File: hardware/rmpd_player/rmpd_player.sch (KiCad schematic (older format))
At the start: 7 parts

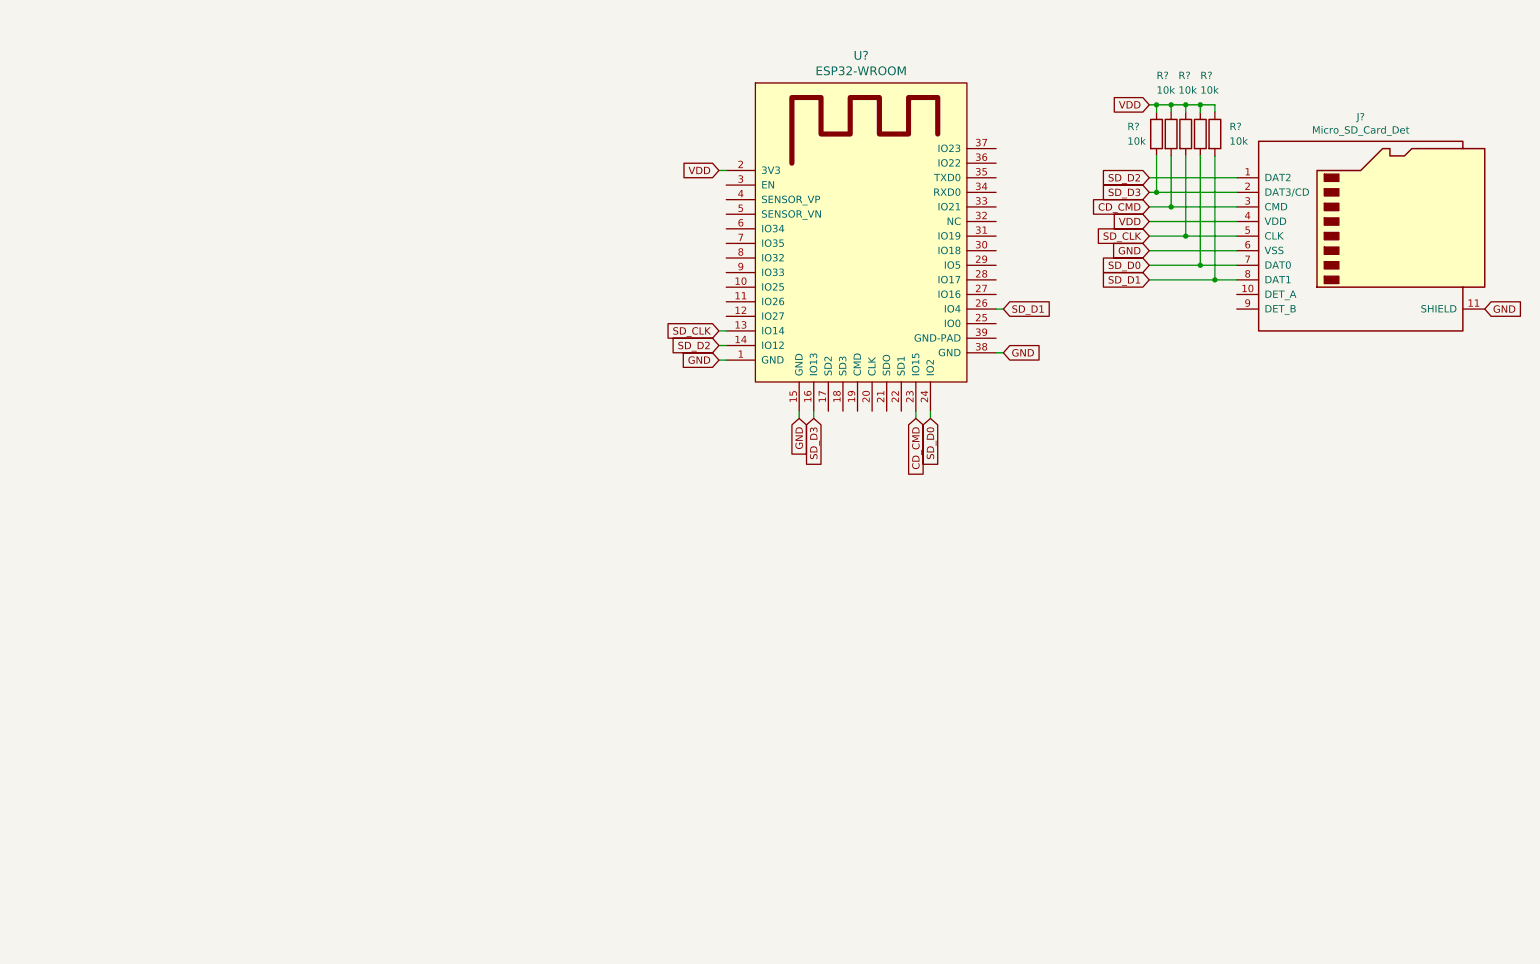
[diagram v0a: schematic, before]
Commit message: more schematic; vs1011 library
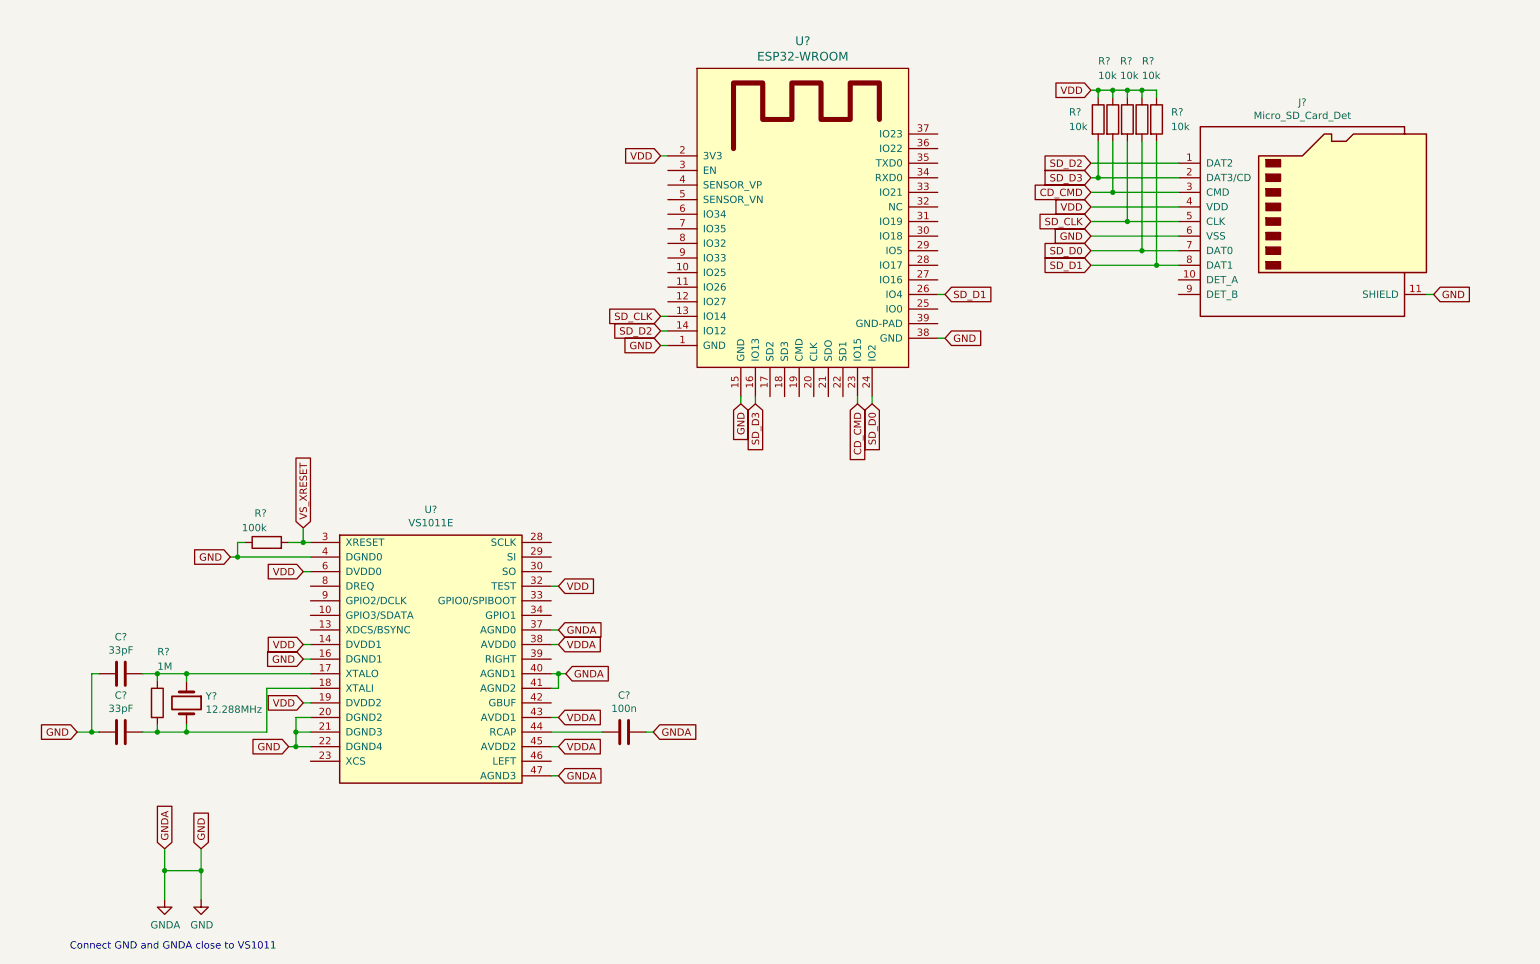
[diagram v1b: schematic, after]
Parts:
- added C? (x2): 33pF, symbol Device:C
- added C?: 100n, symbol Device:C
- added R?: 1M, symbol Device:R
- added R?: 100k, symbol Device:R
- added U?: VS1011E, Housings_QFP:LQFP-48_7x7mm_Pitch0.5mm, symbol vs1011e:VS1011E
- added Y?: 12.288MHz, symbol Device:Crystal
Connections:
- net GND: now also C?.1, C?.2, C?.2, R?.1, U?.16 (DGND1), U?.20 (DGND2), U?.21 (DGND3), U?.22 (DGND4), U?.37 (AGND0), U?.4 (DGND0), U?.40 (AGND1), U?.41 (AGND2), U?.47 (AGND3)
- net VDD: now also U?.14 (DVDD1), U?.19 (DVDD2), U?.32 (TEST), U?.6 (DVDD0)
- new net: C?.1, R?.1, U?.17 (XTALO), Y?.1
- new net: C?.1, R?.2, U?.18 (XTALI), Y?.2
- new net: C?.2, U?.44 (RCAP)
- new net VDDA: U?.38 (AVDD0), U?.43 (AVDD1), U?.45 (AVDD2)
- new net VS_XRESET: R?.2, U?.3 (XRESET)
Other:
- note added: "Connect GND and GNDA close to VS1011"
- moved on the sheet: J?, R?, U?

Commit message: more schematic
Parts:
- added C?: 100n, symbol Device:C
- added C?: 47n, symbol Device:C
- added C? (x2): 10n, symbol Device:C
- added C? (x2): 3n3, symbol Device:C
- added C? (x2): 10.0, symbol Device:CP
- added J?: AudioJack3_Ground, symbol Connector:AudioJack3_Ground
- added R? (x3): 10k, symbol Device:R
- added R?: 10, symbol Device:R
- added R? (x2): 20, symbol Device:R
- added R? (x2): 470, symbol Device:R
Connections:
- net GND: now also C?.2, U?.39 (GND-PAD), C?.1, C?.1, C?.1, C?.1, C?.1, C?.1, J?.S, R?.2, R?.2; no longer C?.1
- net SD_D0: now also U?.25 (IO0)
- net VDD: now also R?.1
- net at U?.3 (EN): now also C?.2, R?.2
- net VS_XDCS: now reaches U?.13 (XDCS/BSYNC)
- net VS_XCS: now reaches U?.23 (XCS)
- net VS_SCLK: now reaches U?.28 (SCLK)
- net VS_SI: now reaches U?.29 (SI)
- net VS_SO: now reaches U?.30 (SO)
- net at U?.39 (RIGHT): now also R?.1, R?.1
- net at U?.42 (GBUF): now also R?.1
- net at U?.44 (RCAP): now also C?.1; no longer C?.2
- net at U?.46 (LEFT): now also R?.1, R?.1
- net VS_DREQ: now reaches U?.8 (DREQ)
- new net: C?.2, R?.2 (x3)
- new net: C?.1, C?.2, R?.2 (x2)
- new net: C?.2, J?.T, R?.1
- new net: C?.2, J?.R, R?.1
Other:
- moved on the sheet: C?, R?, U?, Y?

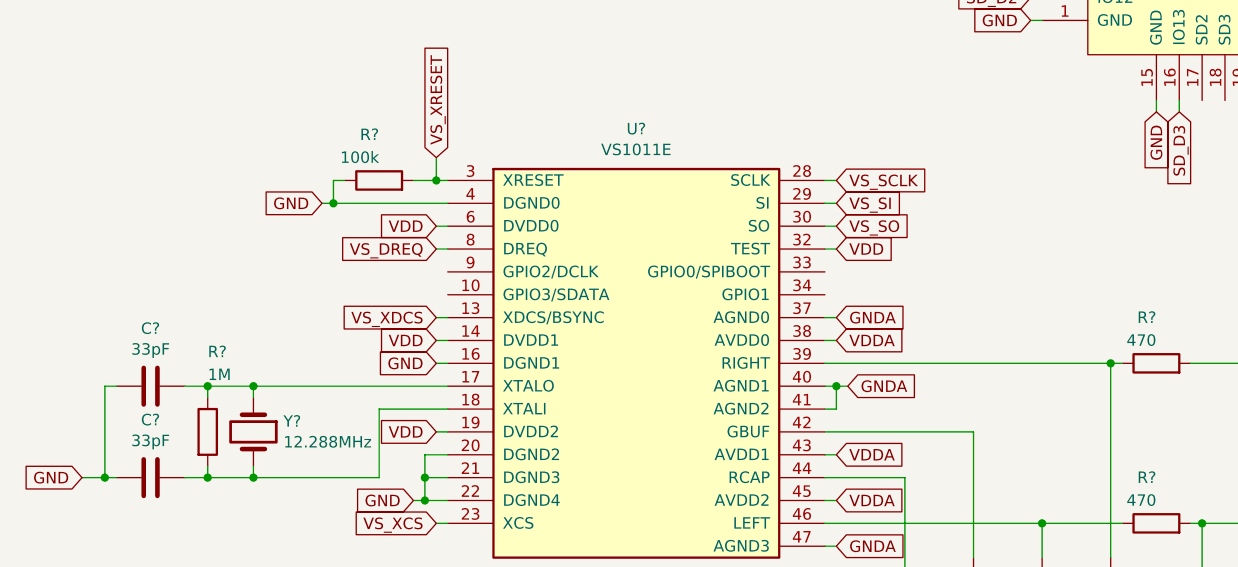
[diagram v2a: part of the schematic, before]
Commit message: 100k pull-downs on gpio vlsi
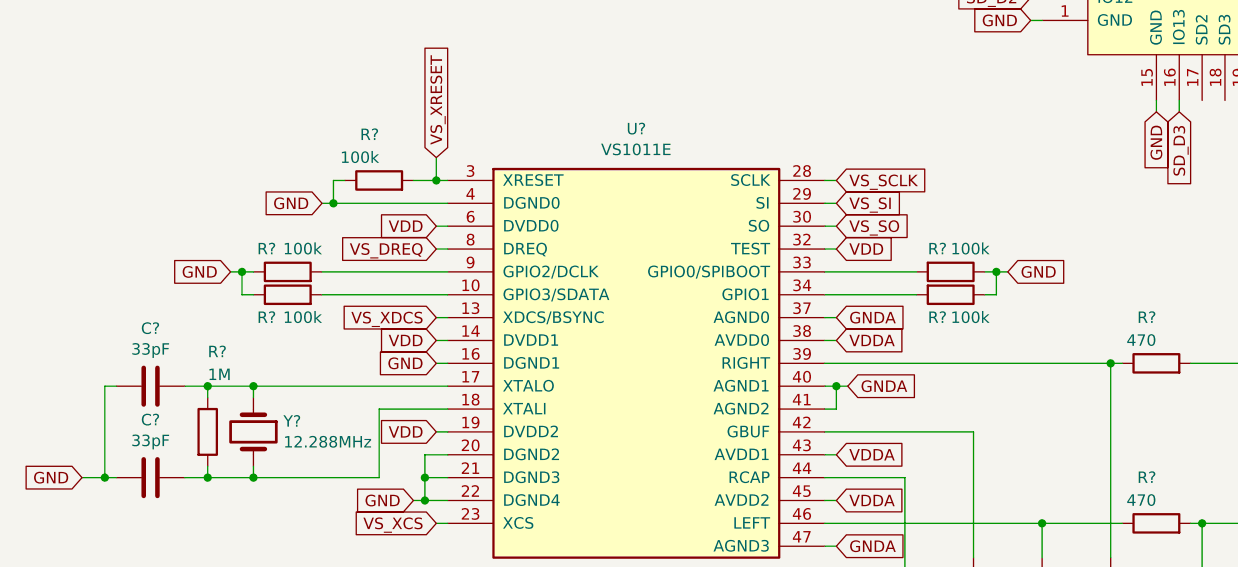
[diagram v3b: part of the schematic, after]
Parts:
- added R? (x4): 100k, symbol Device:R
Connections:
- net GND: now also R?.1, R?.1, R?.1, R?.1
- net at U?.10 (GPIO3/SDATA): now also R?.2
- net at U?.33 (GPIO0/SPIBOOT): now also R?.2
- net at U?.34 (GPIO1): now also R?.2
- net at U?.9 (GPIO2/DCLK): now also R?.2
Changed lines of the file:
@@
 	7050 4900 7100 4900
 Connection ~ 6550 5950
+$Comp
+L Device:R R?
+U 1 1 5C020EC9
+P 1750 4000
+F 0 "R?" V 1850 4050 50  0000 L CNN
+F 1 "100k" V 1850 3850 50  0000 L CNN
+F 2 "" V 1680 4000 50  0001 C CNN
+F 3 "~" H 1750 4000 50  0001 C CNN
+	1    1750 4000
+	0    -1   -1   0
+$EndComp
+$Comp
+L Device:R R?
+U 1 1 5C021253
+P 1750 4100
+F 0 "R?" V 1650 4150 50  0000 L CNN
+F 1 "100k" V 1650 3950 50  0000 L CNN
+F 2 "" V 1680 4100 50  0001 C CNN
+F 3 "~" H 1750 4100 50  0001 C CNN
+	1    1750 4100
+	0    -1   -1   0
+$EndComp
+Wire Wire Line
+	2450 4000 1900 4000
+Wire Wire Line
+	2450 4100 1900 4100
+Wire Wire Line
+	1600 4000 1550 4000
+Wire Wire Line
+	1550 4000 1550 4100
+Wire Wire Line
+	1550 4100 1600 4100
+Text GLabel 1500 4000 0    50   Input ~ 0
+GND
+Wire Wire Line
+	1500 4000 1550 4000
+Connection ~ 1550 4000
+$Comp
+L Device:R R?
+U 1 1 5C03E022
+P 4650 4000
+F 0 "R?" V 4550 3900 50  0000 L CNN
+F 1 "100k" V 4550 4000 50  0000 L CNN
+F 2 "" V 4580 4000 50  0001 C CNN
+F 3 "~" H 4650 4000 50  0001 C CNN
+	1    4650 4000
+	0    1    1    0
+$EndComp
+$Comp
+L Device:R R?
+U 1 1 5C03E122
+P 4650 4100
+F 0 "R?" V 4750 4000 50  0000 L CNN
+F 1 "100k" V 4750 4100 50  0000 L CNN
+F 2 "" V 4580 4100 50  0001 C CNN
+F 3 "~" H 4650 4100 50  0001 C CNN
+	1    4650 4100
+	0    1    1    0
+$EndComp
+Text GLabel 4900 4000 2    50   Input ~ 0
+GND
+Wire Wire Line
+	4100 4000 4500 4000
+Wire Wire Line
+	4500 4100 4100 4100
+Wire Wire Line
+	4800 4000 4850 4000
+Wire Wire Line
+	4800 4100 4850 4100
+Wire Wire Line
+	4850 4100 4850 4000
+Connection ~ 4850 4000
+Wire Wire Line
+	4850 4000 4900 4000
 $EndSCHEMATC

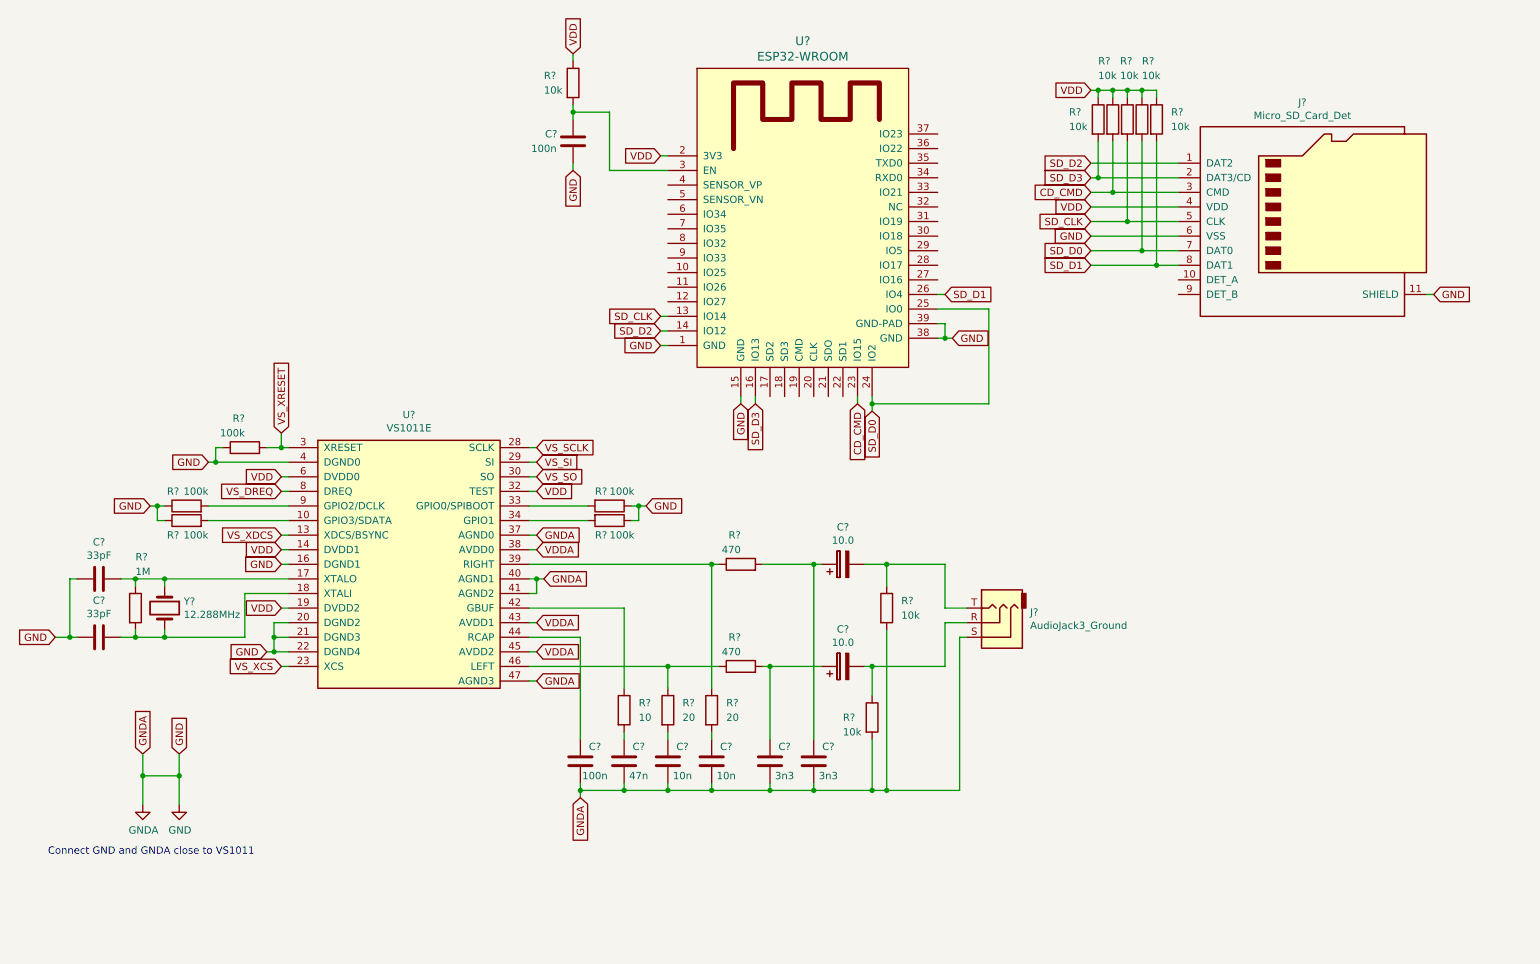
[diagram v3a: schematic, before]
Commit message: spi connection vlsi schematic
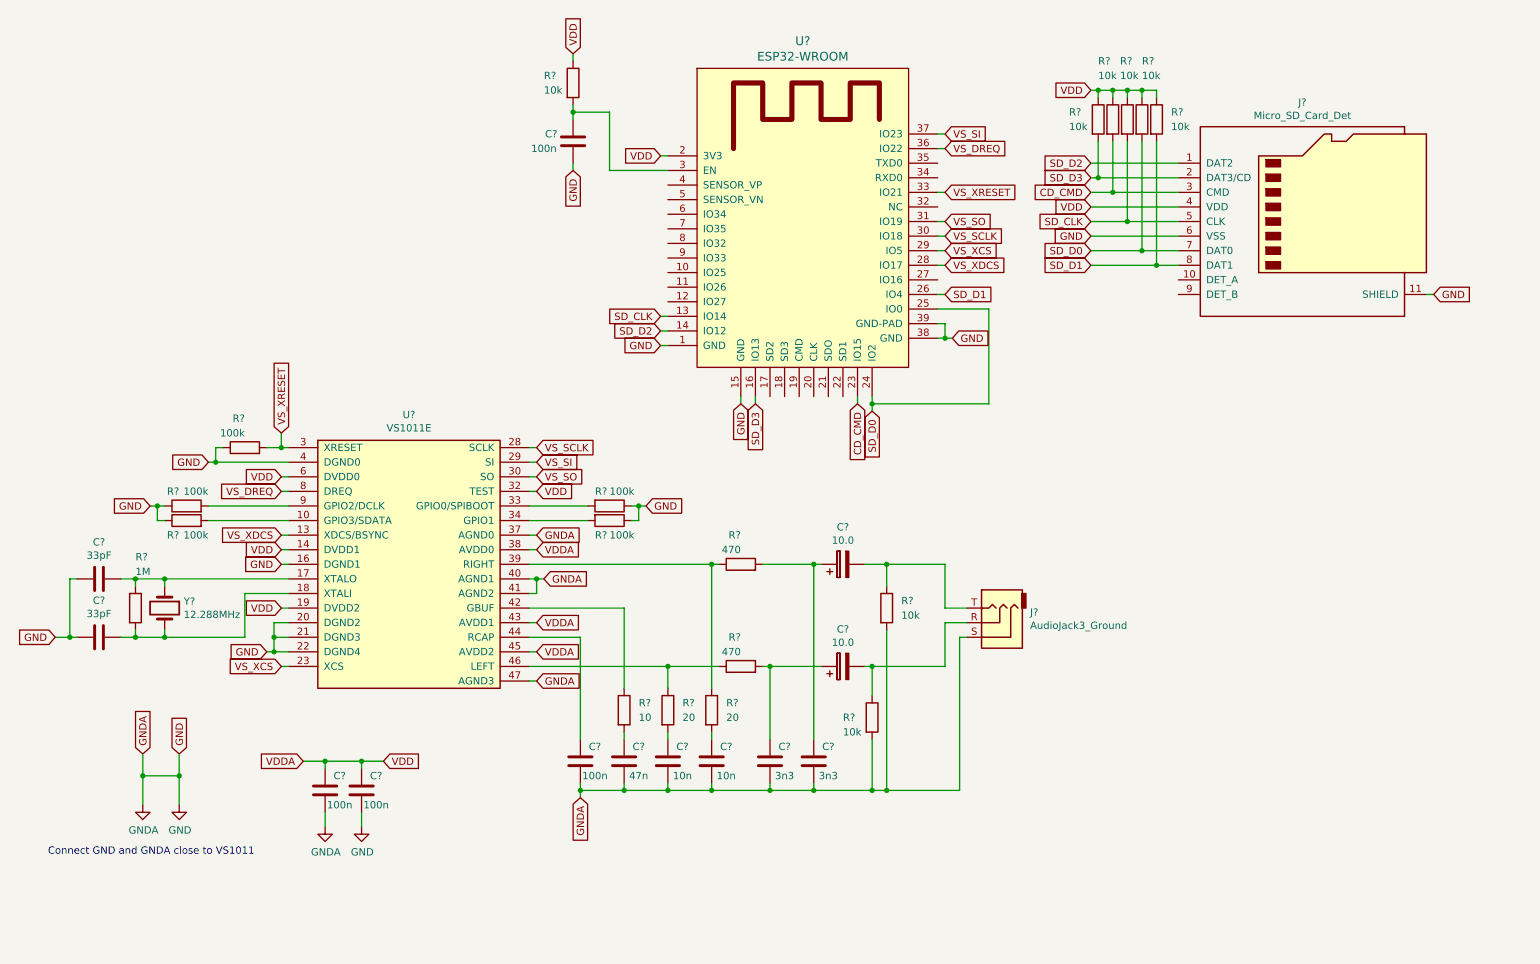
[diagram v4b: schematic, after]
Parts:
- added C? (x2): 100n, symbol Device:C
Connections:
- net VDDA is gone; now on net VDD: U?.38 (AVDD0), U?.43 (AVDD1), U?.45 (AVDD2)
- net GND: now also C?.2, C?.2
- net VDD: now also C?.1, C?.1
- net VS_DREQ: now also U?.36 (IO22)
- net VS_SCLK: now also U?.30 (IO18)
- net VS_SI: now also U?.37 (IO23)
- net VS_SO: now also U?.31 (IO19)
- net VS_XCS: now also U?.29 (IO5)
- net VS_XDCS: now also U?.28 (IO17)
- net VS_XRESET: now also U?.33 (IO21)
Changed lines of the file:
@@
 Wire Wire Line
 	4850 4000 4900 4000
+Text GLabel 6950 2250 2    50   Input ~ 0
+VS_XCS
+Wire Wire Line
+	6950 2250 6900 2250
+Text GLabel 6950 2150 2    50   Input ~ 0
+VS_SCLK
+Text GLabel 6950 2050 2    50   Input ~ 0
+VS_SO
+Text GLabel 6950 1450 2    50   Input ~ 0
+VS_SI
+Wire Wire Line
+	6950 1450 6900 1450
+Wire Wire Line
+	6950 2050 6900 2050
+Wire Wire Line
+	6950 2150 6900 2150
+Text GLabel 6950 1850 2    50   Input ~ 0
+VS_XRESET
+Text GLabel 6950 1550 2    50   Input ~ 0
+VS_DREQ
+Text GLabel 6950 2350 2    50   Input ~ 0
+VS_XDCS
+Wire Wire Line
+	6950 1550 6900 1550
+Wire Wire Line
+	6950 1850 6900 1850
+Wire Wire Line
+	6950 2350 6900 2350
+Text GLabel 2550 5750 0    50   Input ~ 0
+VDDA
+Text GLabel 3100 5750 2    50   Input ~ 0
+VDD
+$Comp
+L Device:C C?
+U 1 1 5C06DB73
+P 2700 5950
+F 0 "C?" H 2800 6050 50  0000 C CNN
+F 1 "100n" H 2800 5850 50  0000 C CNN
+F 2 "" H 2738 5800 50  0001 C CNN
+F 3 "~" H 2700 5950 50  0001 C CNN
+	1    2700 5950
+	1    0    0    -1
+$EndComp
+$Comp
+L Device:C C?
+U 1 1 5C06DC75
+P 2950 5950
+F 0 "C?" H 3050 6050 50  0000 C CNN
+F 1 "100n" H 3050 5850 50  0000 C CNN
+F 2 "" H 2988 5800 50  0001 C CNN
+F 3 "~" H 2950 5950 50  0001 C CNN
+	1    2950 5950
+	1    0    0    -1
+$EndComp
+Wire Wire Line
+	2550 5750 2700 5750
+Wire Wire Line
+	2950 5800 2950 5750
+Connection ~ 2950 5750
+Wire Wire Line
+	2950 5750 3100 5750
+Wire Wire Line
+	2700 5800 2700 5750
+Connection ~ 2700 5750
+Wire Wire Line
+	2700 5750 2950 5750
+$Comp
+L power:GND #PWR?
+U 1 1 5C092AF6
+P 2950 6200
+F 0 "#PWR?" H 2950 5950 50  0001 C CNN
+F 1 "GND" H 2955 6027 50  0000 C CNN
+F 2 "" H 2950 6200 50  0001 C CNN
+F 3 "" H 2950 6200 50  0001 C CNN
+	1    2950 6200
+	1    0    0    -1
+$EndComp
+$Comp
+L power:GNDA #PWR?
+U 1 1 5C092B4B
+P 2700 6200
+F 0 "#PWR?" H 2700 5950 50  0001 C CNN
+F 1 "GNDA" H 2705 6027 50  0000 C CNN
+F 2 "" H 2700 6200 50  0001 C CNN
+F 3 "" H 2700 6200 50  0001 C CNN
+	1    2700 6200
+	1    0    0    -1
+$EndComp
+Wire Wire Line
+	2950 6100 2950 6200
+Wire Wire Line
+	2700 6100 2700 6200
 $EndSCHEMATC
